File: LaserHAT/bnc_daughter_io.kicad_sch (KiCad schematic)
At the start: 11 parts, among them J6 BNC TRIGGER IN, J7 BNC STIM OUT, J8 DB_POWER_TIMING, J9 DB_ANALOG, U8 74LVC2G17

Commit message: LaserHAT + LaserDaughter: one verified "LCSC Part #" field per part for the Fabrication Toolkit
The schematics carried Rev 1 fields under four spellings ("LCSC Part #", "LCSC Part#",
"LCSC Parth#", "LCSC Part") with stale codes (every 0402 resistor = 47k, TLV2371 = AP2171,
74LVC2G17 = SI3134, zeners = SS14, DMMT5401 = MT3608 ...), which is what the toolkit's BOM showed.

- tools/lcsc_parts.py: every code re-verified against LCSC/JLC (MPN, package, value); LEDs to JLC
  basic KT-0603 (D5 white C2290, D7/D9 red C2286; was extended C5336487), R13 3k -> 2k basic,
  U1 CAT24C32 (out of stock) -> M24C32-WDW6TP C283445 (TSSOP-8, pin-compatible), U5 AP2171
  -> the WG-7 SOT-25 variant C110466 (32k in stock vs 250); VALUES table for the changed parts
- tools/stamp_lcsc.py: writes the table into one "LCSC Part #" field per symbol (text patch of
  the KiCad 9 sheets) and footprint (pcbnew), removes the misspelt variants, sets the Values;
  make_laser_daughter.py stamps its output so the laser sheet stays correct on regeneration
- jlc_fab.py warns when a board field disagrees with the table
- both schematics + boards stamped; ERC/DRC unchanged, path_check 0 mismatches; fab outputs
  regenerated; HAT board backup in stash/LaserDriver_user_2026-09-30_pre-lcsc.kicad_pcb

Co-Authored-By: Claude Fable 5.1 <noreply@anthropic.com>
Claude-Session: https://claude.ai/code/session_018vgLizGzYPynnY93ajvoVA
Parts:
- C16: LCSC Part # (none) -> C307331
- D9: LCSC Part # (none) -> C2286
- R18: LCSC Part # (none) -> C4109
- R23: LCSC Part # (none) -> C11702
- R24: LCSC Part # (none) -> C25741
- R25: LCSC Part # (none) -> C25105
- U8: LCSC Part # (none) -> C80500
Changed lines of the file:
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@@
+			)
+		)
+		(property "LCSC Part #" "C25105"
+			(at 157.48 101.6 0)
+			(effects
+				(font
+					(size 1.27 1.27)
+				)
+				(hide yes)
 			)
 		)
@@
 			)
 		)
+		(property "LCSC Part #" "C80500"
+			(at 91.44 139.7 0)
+			(effects
+				(font
+					(size 1.27 1.27)
+				)
+				(hide yes)
+			)
+		)
 		(pin "5"
 		)
@@
 			)
 		)
+		(property "LCSC Part #" "C80500"
+			(at 121.92 60.96 0)
+			(effects
+				(font
+					(size 1.27 1.27)
+				)
+				(hide yes)
+			)
+		)
 		(pin "1"
 		)
@@
 			)
 		)
+		(property "LCSC Part #" "C2286"
+			(at 157.48 127 0)
+			(effects
+				(font
+					(size 1.27 1.27)
+				)
+				(hide yes)
+			)
+		)
 		(pin "1"
 		)
@@
 			)
 		)
+		(property "LCSC Part #" "C4109"
+			(at 157.48 147.32 0)
+			(effects
+				(font
+					(size 1.27 1.27)
+				)
+				(hide yes)
+			)
+		)
 		(pin "1"
 		)
@@
 					(size 1.27 1.27)
 				)
+			)
+		)
+		(property "LCSC Part #" "C11702"
+			(at 76.2 60.96 0)
+			(effects
+				(font
+					(size 1.27 1.27)
+				)
+				(hide yes)
 			)
 		)
@@
 			)
 		)
+		(property "LCSC Part #" "C80500"
+			(at 121.92 101.6 0)
+			(effects
+				(font
+					(size 1.27 1.27)
+				)
+				(hide yes)
+			)
+		)
 		(pin "3"
 		)
@@
 			)
 		)
+		(property "LCSC Part #" "C307331"
+			(at 106.68 139.7 0)
+			(effects
+				(font
+					(size 1.27 1.27)
+				)
+				(hide yes)
+			)
+		)
 		(pin "1"
 		)
@@
 			)
 		)
+		(property "LCSC Part #" "C25741"
+			(at 91.44 71.12 0)
+			(effects
+				(font
+					(size 1.27 1.27)
+				)
+				(hide yes)
+			)
+		)

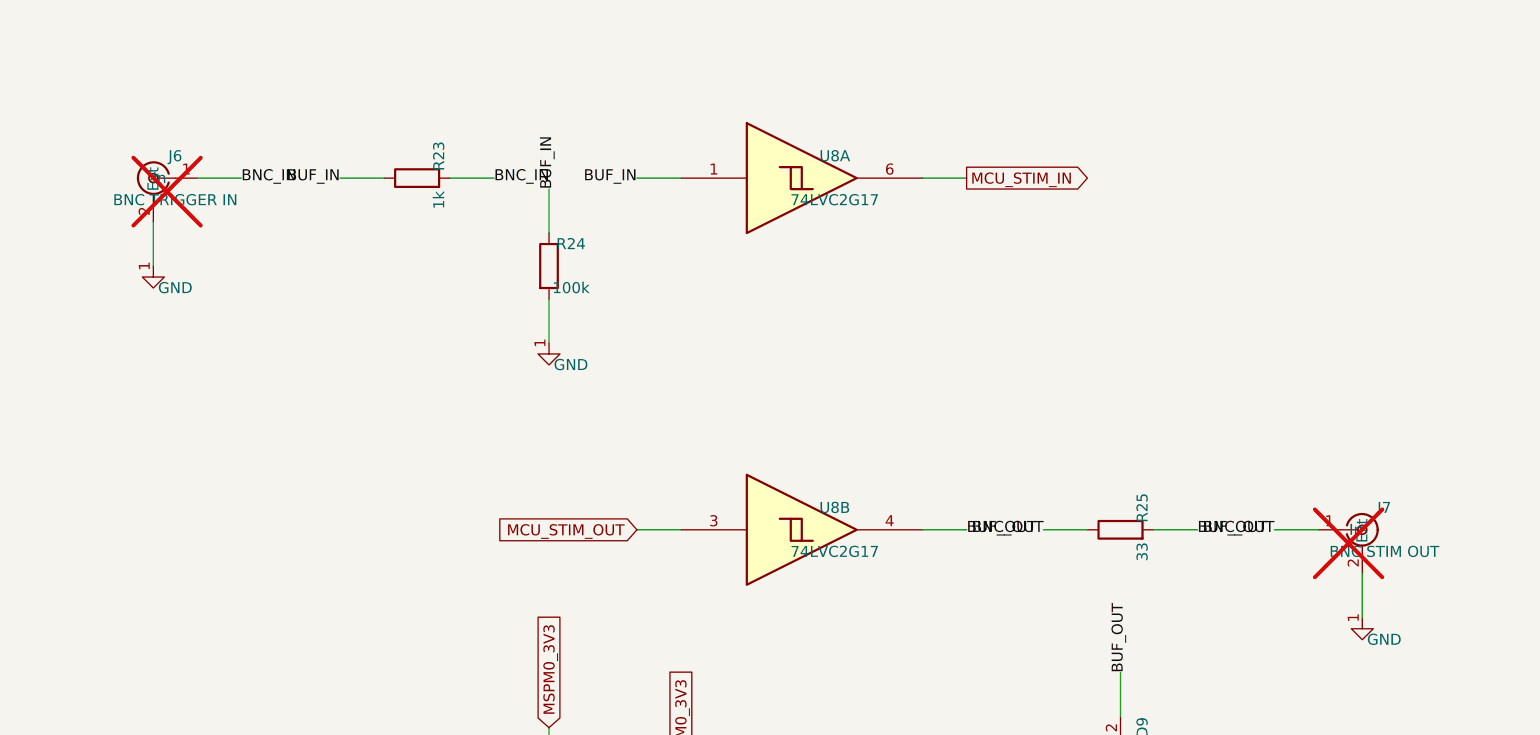
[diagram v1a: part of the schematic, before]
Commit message: Fab flags: DNP = not populated, hand-fitted = no part number + exclude from position files
The schematic DNP attribute had been doing double duty ("JLC doesn't place it" for the Pi header,
BNCs and the laser-diode socket, and "not fitted"). KiCad has a flag for each:
- lcsc_parts.NOT_FITTED -> symbol DNP (schematic, carried to the board): HAT R1/R2, the ID_SD/ID_SC
  pull-ups the Pi already provides
- lcsc_parts.HAND_FIT -> DNP cleared, no "LCSC Part #", footprint attribute "exclude from position
  files" (board-only): HAT J1/J6/J7/J8/J9/SW8, laser J1/J2/J3/J5, e-stim J1/J8/J9. They stay in the
  Fabrication Toolkit BOM with an empty number, which JLC's upload shows as "do not place".
stamp_lcsc.py applies both (e-stim board: flags only, its own "LCSC" fields untouched);
jlc_fab.py lists "Hand-fitted" and "Not fitted (DNP)" separately and accepts the toolkit's field
names. HAT now 42 placements / 28 unique. ERC/DRC/path_check unchanged; fab outputs regenerated.

Co-Authored-By: Claude Fable 5.1 <noreply@anthropic.com>
Claude-Session: https://claude.ai/code/session_018vgLizGzYPynnY93ajvoVA
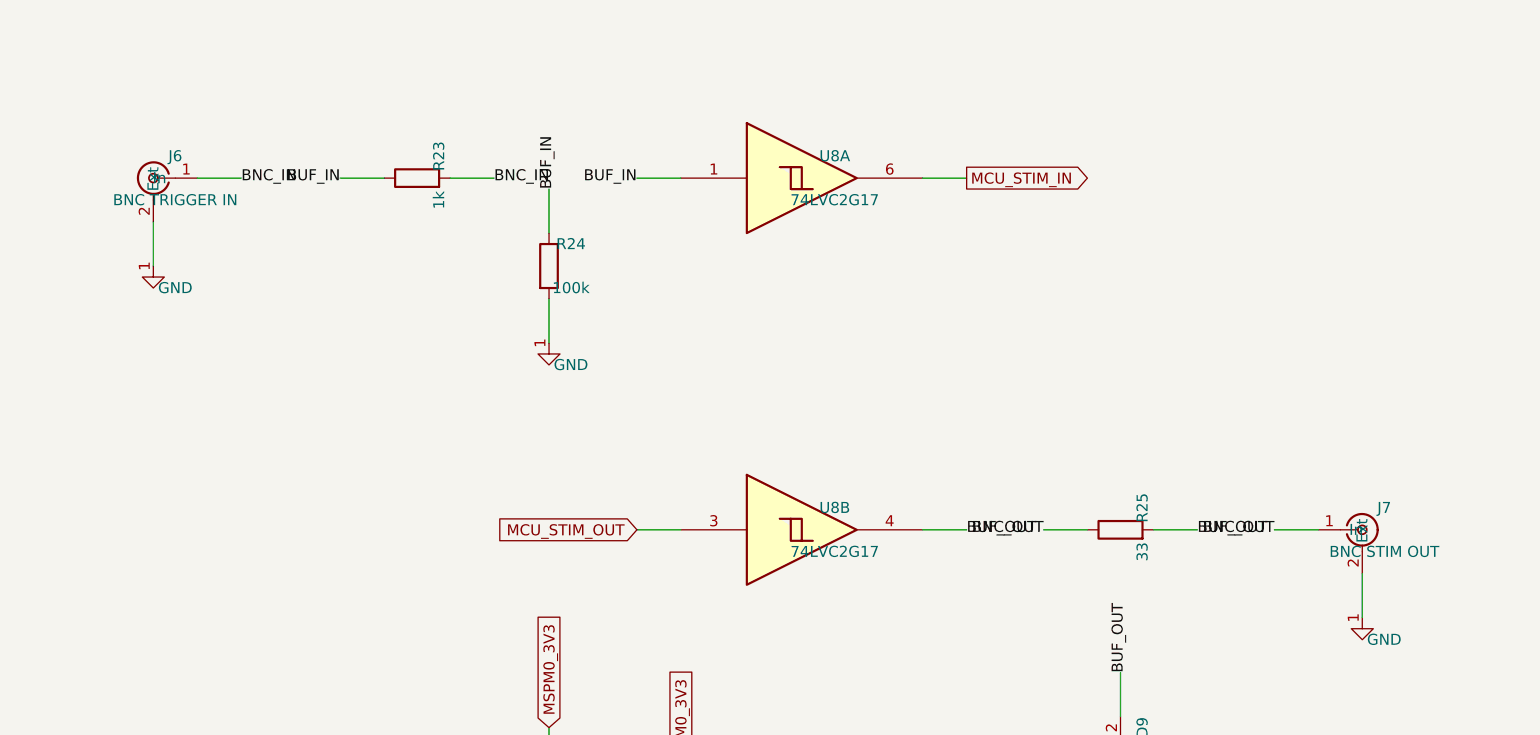
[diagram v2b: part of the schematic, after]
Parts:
- J6, J7: now fitted
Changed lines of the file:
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@@
 		(in_bom yes)
 		(on_board yes)
-		(dnp yes)
+		(dnp no)
 		(fields_autoplaced yes)
 		(property "Reference" "J7"
@@
 		(in_bom yes)
 		(on_board yes)
-		(dnp yes)
+		(dnp no)
 		(fields_autoplaced yes)
 		(property "Reference" "J6"

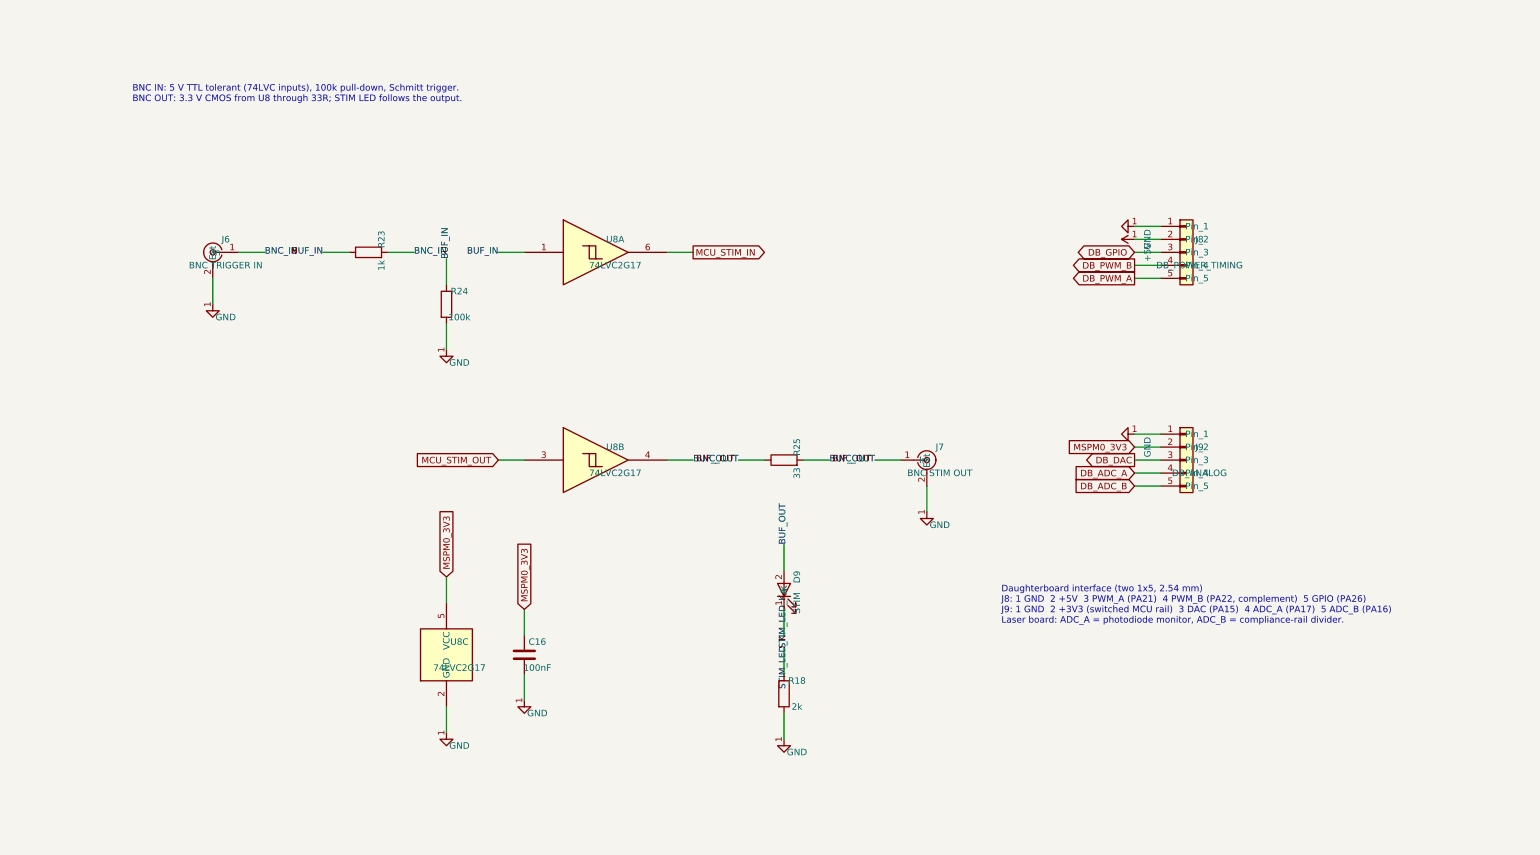
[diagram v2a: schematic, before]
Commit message: BOM: descriptions from the LCSC catalog, value verifier and netlist-vs-board check on all three boards
R15 (2k, C4109) still said "200Ω" in its Description: the Rev 1 symbols carried descriptions and
datasheet links of parts long replaced (R13 "1kΩ", D5 "Emerald Green", D7 "Ice Blue", L1 "22uH 6x6",
Rs1 "10Ω", D3 "1N4148", ...). Now:
- tools/lcsc_catalog.json: LCSC MPN, brand, package, description, parameter table (Resistance /
  Capacitance / Inductance ...) and datasheet URL for every code, fetched by tools/lcsc_verify.py
- stamp_lcsc.py writes Description "<MPN> (<brand>, <package>): <LCSC description>" and the LCSC
  datasheet URL into every machine-placed symbol and footprint (HAT + laser)
- tools/lcsc_verify.py: every R/C/L Value must equal LCSC's parameter, other parts' MPN must match
  the Value (label values like "FIRE" are listed, not failed), size codes must match the package;
  covers HAT, laser and the e-stim list (bom_EStimDaughter.csv) and the fields the toolkit reads:
  0 mismatches on all three boards
- tools/sync_check.py: read-only F8 (parts, footprint ids, values, DNP, pad nets, paths vs the
  exported netlist): 0 differences on all three boards after fixing the owl's missing
  "Footprints:" library prefix and the e-stim U5/U8 paths (netlist uses the other unit's uuid;
  backup in stash/EStimDaughter_2026-09-30_pre-unitpath.kicad_pcb)
- values: laser D1/D3 "SS14" -> "DSK14" (the part ordered), HAT J5 -> "GT-USB-7010ASV"
- fab outputs regenerated; ERC/DRC unchanged

Co-Authored-By: Claude Fable 5.1 <noreply@anthropic.com>
Claude-Session: https://claude.ai/code/session_018vgLizGzYPynnY93ajvoVA
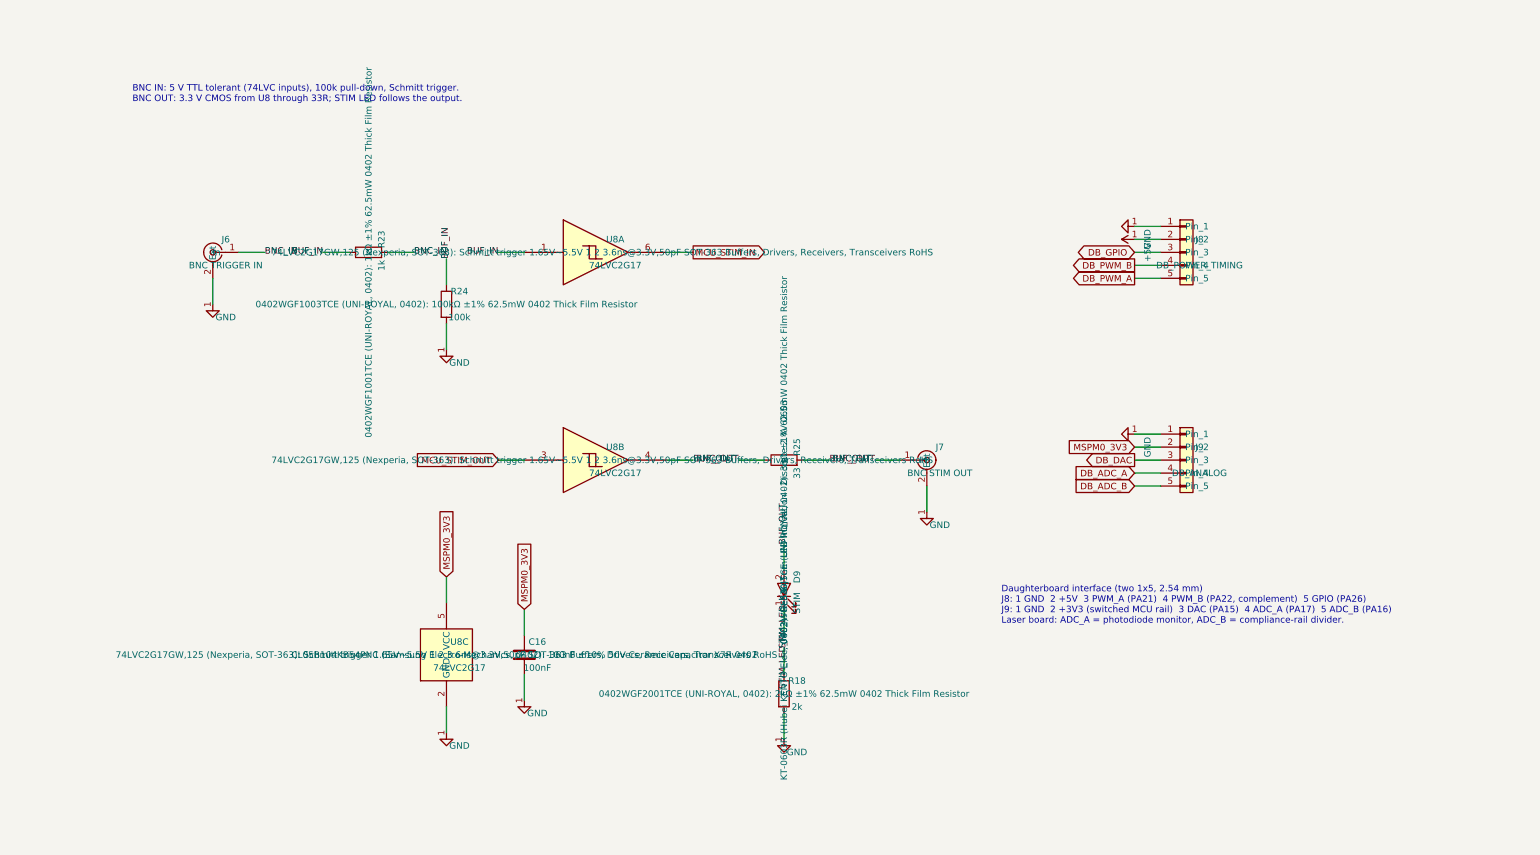
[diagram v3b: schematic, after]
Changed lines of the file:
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@@
 			)
 		)
-		(property "Datasheet" ""
+		(property "Datasheet" "https://datasheet.lcsc.com/datasheet/pdf/0a975aaa49b7c97f38a963127be4a823.pdf?productCode=C25105"
 			(at 157.48 101.6 0)
 			(effects
@@
 			)
 		)
-		(property "Description" ""
+		(property "Description" "0402WGF330JTCE (UNI-ROYAL, 0402): 33Ω ±1% 62.5mW 0402 Thick Film Resistor"
 			(at 157.48 101.6 0)
 			(effects
@@
 			)
 		)
-		(property "Datasheet" ""
+		(property "Datasheet" "https://datasheet.lcsc.com/datasheet/pdf/df73e86b8822ee2ea9fc0915b8db982b.pdf?productCode=C80500"
 			(at 91.44 139.7 0)
 			(effects
@@
 			)
 		)
-		(property "Description" ""
+		(property "Description" "74LVC2G17GW,125 (Nexperia, SOT-363): Schmitt trigger 1.65V~5.5V 1 2 3.6ns@3.3V,50pF SOT-363 Buffers, Drivers, Receivers, Transceivers RoHS"
 			(at 91.44 139.7 0)
 			(effects
@@
 			)
 		)
-		(property "Datasheet" ""
+		(property "Datasheet" "https://datasheet.lcsc.com/datasheet/pdf/df73e86b8822ee2ea9fc0915b8db982b.pdf?productCode=C80500"
 			(at 121.92 60.96 0)
 			(effects
@@
 			)
 		)
-		(property "Description" ""
+		(property "Description" "74LVC2G17GW,125 (Nexperia, SOT-363): Schmitt trigger 1.65V~5.5V 1 2 3.6ns@3.3V,50pF SOT-363 Buffers, Drivers, Receivers, Transceivers RoHS"
 			(at 121.92 60.96 0)
 			(effects
@@
 			)
 		)
-		(property "Datasheet" ""
+		(property "Datasheet" "https://datasheet.lcsc.com/datasheet/pdf/011ec3e8cb1e825f6961d29bc4db4c7a.pdf?productCode=C2286"
 			(at 157.48 127 0)
 			(effects
@@
 			)
 		)
-		(property "Description" ""
+		(property "Description" "KT-0603R (Hubei KENTO Elec, 0603): Red 645nm LED Indication - Discrete 2.4V 0603"
 			(at 157.48 127 0)
 			(effects
@@
 			)
 		)
-		(property "Datasheet" ""
+		(property "Datasheet" "https://datasheet.lcsc.com/datasheet/pdf/0a975aaa49b7c97f38a963127be4a823.pdf?productCode=C4109"
 			(at 157.48 147.32 0)
 			(effects
@@
 			)
 		)
-		(property "Description" ""
+		(property "Description" "0402WGF2001TCE (UNI-ROYAL, 0402): 2kΩ ±1% 62.5mW 0402 Thick Film Resistor"
 			(at 157.48 147.32 0)
 			(effects
@@
 			)
 		)
-		(property "Datasheet" ""
+		(property "Datasheet" "https://datasheet.lcsc.com/datasheet/pdf/0a975aaa49b7c97f38a963127be4a823.pdf?productCode=C11702"
 			(at 76.2 60.96 0)
 			(effects
@@
 			)
 		)
-		(property "Description" ""
+		(property "Description" "0402WGF1001TCE (UNI-ROYAL, 0402): 1kΩ ±1% 62.5mW 0402 Thick Film Resistor"
 			(at 76.2 60.96 0)
 			(effects
@@
 			)
 		)
-		(property "Datasheet" ""
+		(property "Datasheet" "https://datasheet.lcsc.com/datasheet/pdf/df73e86b8822ee2ea9fc0915b8db982b.pdf?productCode=C80500"
 			(at 121.92 101.6 0)
 			(effects
@@
 			)
 		)
-		(property "Description" ""
+		(property "Description" "74LVC2G17GW,125 (Nexperia, SOT-363): Schmitt trigger 1.65V~5.5V 1 2 3.6ns@3.3V,50pF SOT-363 Buffers, Drivers, Receivers, Transceivers RoHS"
 			(at 121.92 101.6 0)
 			(effects
@@
 			)
 		)
-		(property "Datasheet" ""
+		(property "Datasheet" "https://datasheet.lcsc.com/datasheet/pdf/02336ea48ea44ca18c72517dd3cb7b47.pdf?productCode=C307331"
 			(at 106.68 139.7 0)
 			(effects
@@
 			)
 		)
-		(property "Description" ""
+		(property "Description" "CL05B104KB54PNC (Samsung Electro-Mechanics, 0402): 100nF ±10% 50V Ceramic Capacitor X7R 0402"
 			(at 106.68 139.7 0)
 			(effects
@@
 			)
 		)
-		(property "Datasheet" ""
+		(property "Datasheet" "https://datasheet.lcsc.com/datasheet/pdf/0a975aaa49b7c97f38a963127be4a823.pdf?productCode=C25741"
 			(at 91.44 71.12 0)
 			(effects
@@
 			)
 		)
-		(property "Description" ""
+		(property "Description" "0402WGF1003TCE (UNI-ROYAL, 0402): 100kΩ ±1% 62.5mW 0402 Thick Film Resistor"
 			(at 91.44 71.12 0)
 			(effects

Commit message: Fab: nothing JLC does not place may be in its BOM (hand-fitted and DNP parts excluded from BOM too)
JLC's upload rejects "R2,SW8,J1,J6,J7,J8,R1,J9 designators don't exist in the CPL file": a BOM
line without a placement is an error, not a "do not place". So HAND_FIT parts now carry symbol
"exclude from BOM" + footprint exclude-from-BOM and -position-files, NOT_FITTED parts DNP +
exclude-from-BOM (independent of the toolkit's "Exclude DNP" checkbox), e-stim PS1 likewise on
its board. jlc_fab.py classifies from lcsc_parts.HAND_FIT and warns on any flag drift.
Verified with the toolkit's own ProcessManager in both checkbox states: every BOM designator is
in the CPL on all three boards (HAT 30 lines / 42, laser 20 / 23, e-stim 23 / 42).

Co-Authored-By: Claude Fable 5.1 <noreply@anthropic.com>
Claude-Session: https://claude.ai/code/session_018vgLizGzYPynnY93ajvoVA
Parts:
- J6, J7, J8, J9: now left out of the parts list
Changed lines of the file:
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@@
 		(unit 1)
 		(exclude_from_sim no)
-		(in_bom yes)
+		(in_bom no)
 		(on_board yes)
 		(dnp no)
@@
 		(unit 1)
 		(exclude_from_sim no)
-		(in_bom yes)
+		(in_bom no)
 		(on_board yes)
 		(dnp no)
@@
 		(unit 1)
 		(exclude_from_sim no)
-		(in_bom yes)
+		(in_bom no)
 		(on_board yes)
 		(dnp no)
@@
 		(unit 1)
 		(exclude_from_sim no)
-		(in_bom yes)
-		(on_board yes)
-		(dnp no)
+		(in_bom no)
+		(on_board yes)
+		(dnp no)
